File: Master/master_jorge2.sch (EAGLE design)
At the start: 51 parts, among them J1 ISP, K1 653002114822, K2 653002114822, K3 653002114822, K4 653002114822, U1 ATMEGA128RFA1, U2 TPS73633-DBVT, U3 ULN2003ADR, U4 LSM303D, U5 L3GD20H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

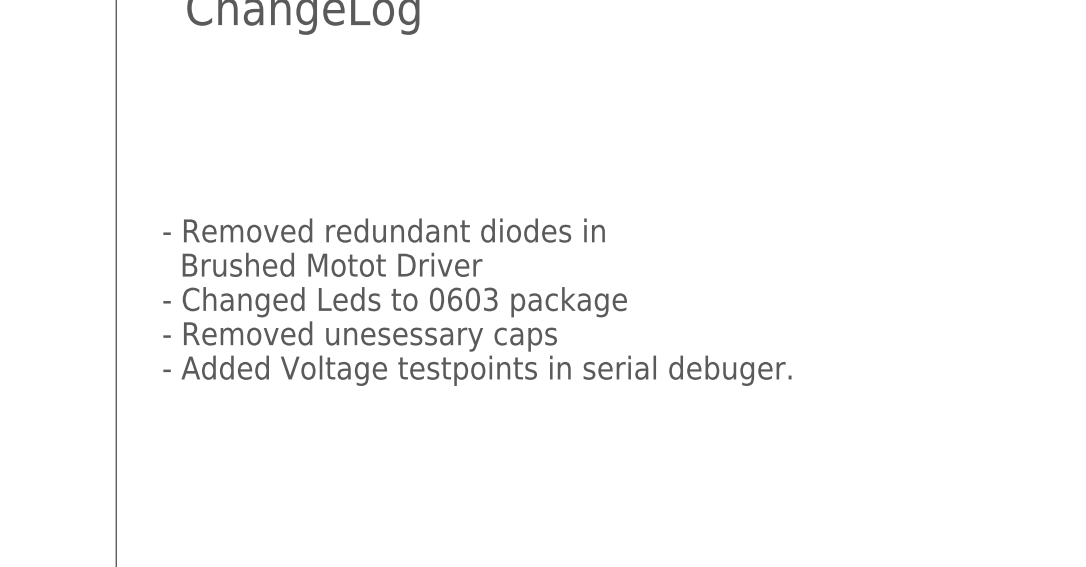
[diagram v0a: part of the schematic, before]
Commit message: Adding New schematic/board
Adding new schematic and board. The new board contains a different
border line  for placing the motors directly in the pcb.
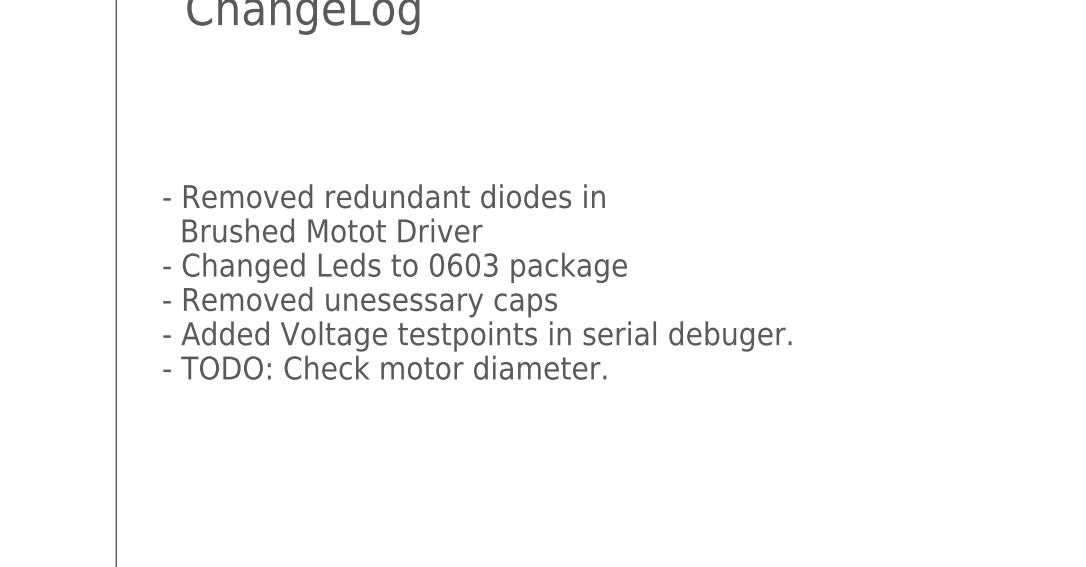
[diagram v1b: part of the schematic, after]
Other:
- note added: "- Removed redundant diodes in Brushed Motot Driver - Changed Leds to 0603 package - Removed unesessary caps - Added Voltage testpoints in serial debuger. - TODO: Check motor diameter."
- note removed: "- Removed redundant diodes in Brushed Motot Driver - Changed Leds to 0603 package - Removed unesessary caps - Added Voltage testpoints in serial debuger."
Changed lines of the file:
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@@
 - Removed unesessary caps
 - Added Voltage testpoints in serial debuger.
-</text>
+- TODO: Check motor diameter. </text>
 </plain>
 <instances>
